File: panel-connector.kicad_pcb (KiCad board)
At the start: 2 copper layers, 95.9 x 90.2 mm, 201 parts, among them J1 PC104-8BIT, J105 MOLEX_FFC-14, J2 PC104PTH, J200 MOLEX_FFC-14, J201 CONN-TAB, J202 CONN-TAB, J203 CONN-TAB, J204 CONN-TAB, J210 MOLEX_FFC-14, J211 CONN-TAB, J212 CONN-TAB, J213 CONN-TAB, J214 CONN-TAB, J220 MOLEX_FFC-14, J221 CONN-TAB, J222 CONN-TAB, J223 CONN-TAB, J224 CONN-TAB, J230 MOLEX_FFC-14, J231 CONN-TAB, J232 CONN-TAB, J233 CONN-TAB, J234 CONN-TAB, J3 PC104PTH, J4 PC104PTH, J5 PC104PTH, J6 OEM719, U100 SPV1040, U110 SPV1040, U120 SPV1040, U130 SPV1040, U140 SPV1040, U150 SPV1040, U160 SPV1040, U170 SPV1040, U200 ADG728, U210 ADG728, U220 ADG728, U230 ADG728

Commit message: placed mppt circuits
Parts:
- C100, C101, C102, C103, C104, C105, C110, C111, C112, C113, C114, C115, C120, C121, C122, C123, C124, C125, C130, C131, C132, C133, C134, C135, C140, C141, C142, C143, C144, C145, C150, C151, C152, C153, C154, C155, C160, C161, C162, C163, C164, C165, C170, C171, C172, C173, C174, C175, C211, C212, C221, C222, C231, C232, D100, D110, D120, D130, D140, D150, D160, D170, J105, J200, J201, J202, J203, J204, J210, J220, J230, L100, L110, L120, L130, L140, L150, L160, L170, R100, R101, R102, R103, R104, R105, R106, R110, R111, R112, R113, R114, R115, R116, R120, R121, R122, R123, R124, R125, R126, R130, R131, R132, R133, R134, R135, R136, R140, R141, R142, R143, R144, R145, R146, R150, R151, R152, R153, R154, R155, R156, R160, R161, R162, R163, R164, R165, R166, R170, R171, R172, R173, R174, R175, R176, R210, R211, R212, R213, R214, R215, R220, R221, R222, R223, R224, R225, R230, R231, R232, R233, R234, R235, U100, U110, U120, U130, U140, U150, U160, U170, U210, U220, U230: moved to B.Cu
- moved R106 198.6 mm to (159.0, 99.6), turned to 270 degrees
- moved C104 198.4 mm to (161.9, 102.3), turned to 180 degrees
- moved C102 195.9 mm to (160.9, 99.6), turned to 270 degrees
- moved R103 193.4 mm to (159.8, 96.7), turned to 0 degrees
- moved R105 193.1 mm to (162.9, 99.6), turned to 90 degrees
- moved R102 190.7 mm to (159.8, 94.8), turned to 0 degrees
- moved R104 189.7 mm to (167.7, 101.9), turned to 180 degrees
- moved C103 187.9 mm to (162.7, 95.7), turned to 270 degrees
- moved C105 185.9 mm to (168.2, 99.8), turned to 180 degrees
- moved U100 181.3 mm to (168.1, 96.4), turned to 180 degrees
- moved D100 181.0 mm to (172.6, 100.7), turned to 180 degrees
- moved R101 180.7 mm to (166.0, 93.8), turned to 0 degrees
- moved D160 178.3 mm to (173.7, 56.4), turned to 270 degrees
- moved L160 176.3 mm to (168.0, 54.1), turned to 0 degrees
- moved R164 176.2 mm to (174.9, 61.3), turned to 270 degrees
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- renumbered R201'1 to R201
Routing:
- net (no net): track 26.0 -> 0.00 mm
- net GND: track 36.9 -> 55.9 mm, vias 32 -> 48
- net /3V3: track 0.00 -> 11.9 mm
- net /Port_X-/A1: track 0.00 -> 3.52 mm
- net /Port_Y-/A1: track 0.00 -> 3.52 mm
- net /Port_X+/A1: track 0.00 -> 3.52 mm
- net /Port_Y+/A1: track 0.00 -> 3.52 mm
- net /Port_Y-/A0: track 0.00 -> 3.38 mm
- net /Port_X-/A0: track 0.00 -> 3.38 mm
- net /Port_Y+/A0: track 0.00 -> 3.38 mm
- net /Port_X+/A0: track 0.00 -> 3.38 mm
- net /SENSOR_Y+: track 0.00 -> 3.00 mm
- net /SENSOR_X-: track 0.00 -> 3.00 mm
- net /SENSOR_Y-: track 0.00 -> 3.00 mm
- net /SENSOR_X+: track 0.00 -> 3.00 mm
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- added copper zone on B.Cu, net /MPPT_X+_1/LX
- added copper zone on B.Cu, net /MPPT_X+_1/MPPT_OUT
- added copper zone on B.Cu, net /MPPT_X+_1/PV+
- added copper zone on B.Cu, net /MPPT_X+_1/VOUT+
- added copper zone on B.Cu, net /MPPT_X+_2/LX
- added copper zone on B.Cu, net /MPPT_X+_2/MPPT_OUT
- added copper zone on B.Cu, net /MPPT_X+_2/PV+
- added copper zone on B.Cu, net /MPPT_X-_1/LX
- added copper zone on B.Cu, net /MPPT_X-_1/MPPT_OUT
- added copper zone on B.Cu, net /MPPT_X-_1/PV+
- added copper zone on B.Cu, net /MPPT_X-_2/LX
- added copper zone on B.Cu, net /MPPT_X-_2/MPPT_OUT
- added copper zone on B.Cu, net /MPPT_X-_2/PV+
- added copper zone on B.Cu, net /MPPT_Y+_1/LX
- added copper zone on B.Cu, net /MPPT_Y+_1/MPPT_OUT
- added copper zone on B.Cu, net /MPPT_Y+_1/PV+
- added copper zone on B.Cu, net /MPPT_Y+_2/LX
- added copper zone on B.Cu, net /MPPT_Y+_2/MPPT_OUT
- added copper zone on B.Cu, net /MPPT_Y+_2/PV+
- added copper zone on B.Cu, net /MPPT_Y-_1/LX
- added copper zone on B.Cu, net /MPPT_Y-_1/MPPT_OUT
- added copper zone on B.Cu, net /MPPT_Y-_1/PV+
- added copper zone on B.Cu, net /MPPT_Y-_2/LX
- added copper zone on B.Cu, net /MPPT_Y-_2/MPPT_OUT
- added copper zone on B.Cu, net /MPPT_Y-_2/PV+
- added copper zone on F.Cu, net GND
- removed copper zone on F.Cu, net /MPPT_X+_1/LX
- removed copper zone on F.Cu, net /MPPT_X+_1/MPPT_OUT
- removed copper zone on F.Cu, net /MPPT_X+_1/PV+
- removed copper zone on F.Cu, net /MPPT_X+_1/VOUT+
- removed copper zone on F.Cu, net /MPPT_X+_2/LX
- removed copper zone on F.Cu, net /MPPT_X+_2/MPPT_OUT
- removed copper zone on F.Cu, net /MPPT_X+_2/PV+
- removed copper zone on F.Cu, net /MPPT_X-_1/LX
- removed copper zone on F.Cu, net /MPPT_X-_1/MPPT_OUT
- removed copper zone on F.Cu, net /MPPT_X-_1/PV+
- removed copper zone on F.Cu, net /MPPT_X-_2/LX
- removed copper zone on F.Cu, net /MPPT_X-_2/MPPT_OUT
- removed copper zone on F.Cu, net /MPPT_X-_2/PV+
- removed copper zone on F.Cu, net /MPPT_Y+_1/LX
- removed copper zone on F.Cu, net /MPPT_Y+_1/MPPT_OUT
- removed copper zone on F.Cu, net /MPPT_Y+_1/PV+
- removed copper zone on F.Cu, net /MPPT_Y+_2/LX
- removed copper zone on F.Cu, net /MPPT_Y+_2/MPPT_OUT
- removed copper zone on F.Cu, net /MPPT_Y+_2/PV+
- removed copper zone on F.Cu, net /MPPT_Y-_1/LX
- removed copper zone on F.Cu, net /MPPT_Y-_1/MPPT_OUT
- removed copper zone on F.Cu, net /MPPT_Y-_1/PV+
- removed copper zone on F.Cu, net /MPPT_Y-_2/LX
- removed copper zone on F.Cu, net /MPPT_Y-_2/MPPT_OUT
- removed copper zone on F.Cu, net /MPPT_Y-_2/PV+
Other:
- board text removed: "GPS Coax slot location and dimentions are provisional. Consider structural integrity of the board with cables connected."

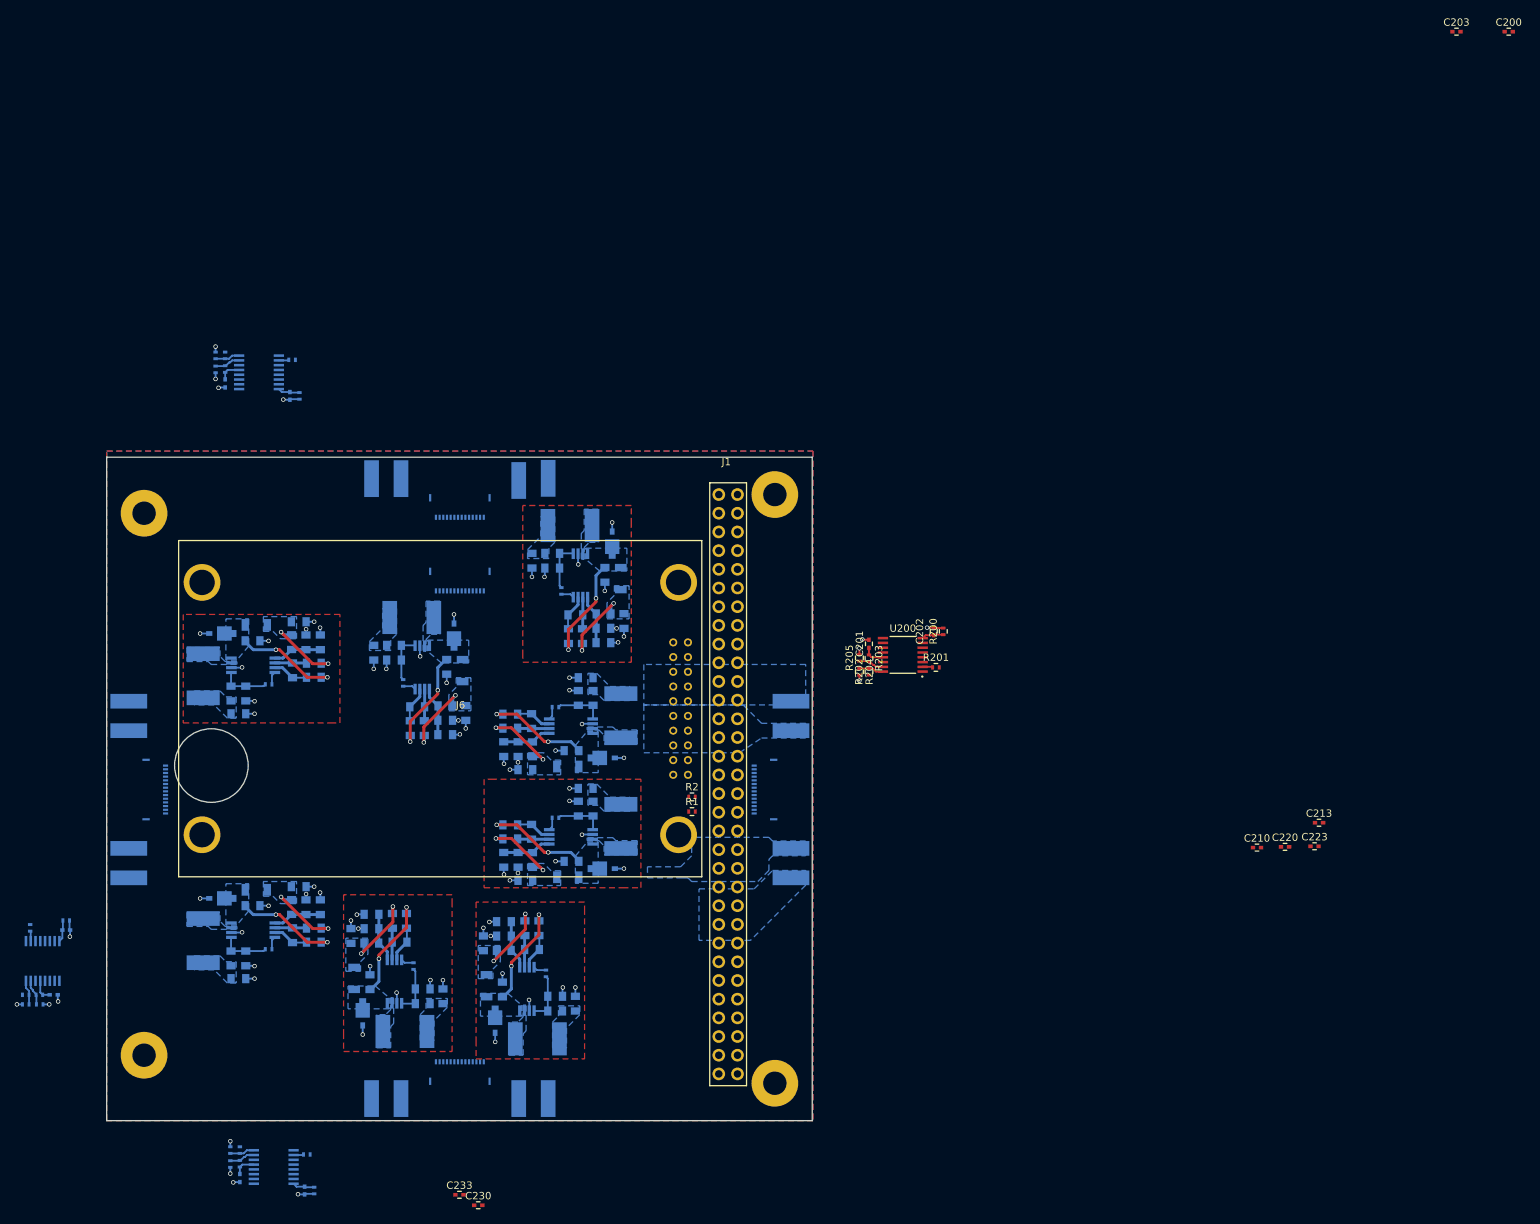
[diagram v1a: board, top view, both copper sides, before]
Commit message: routing complete except for GPS_RST
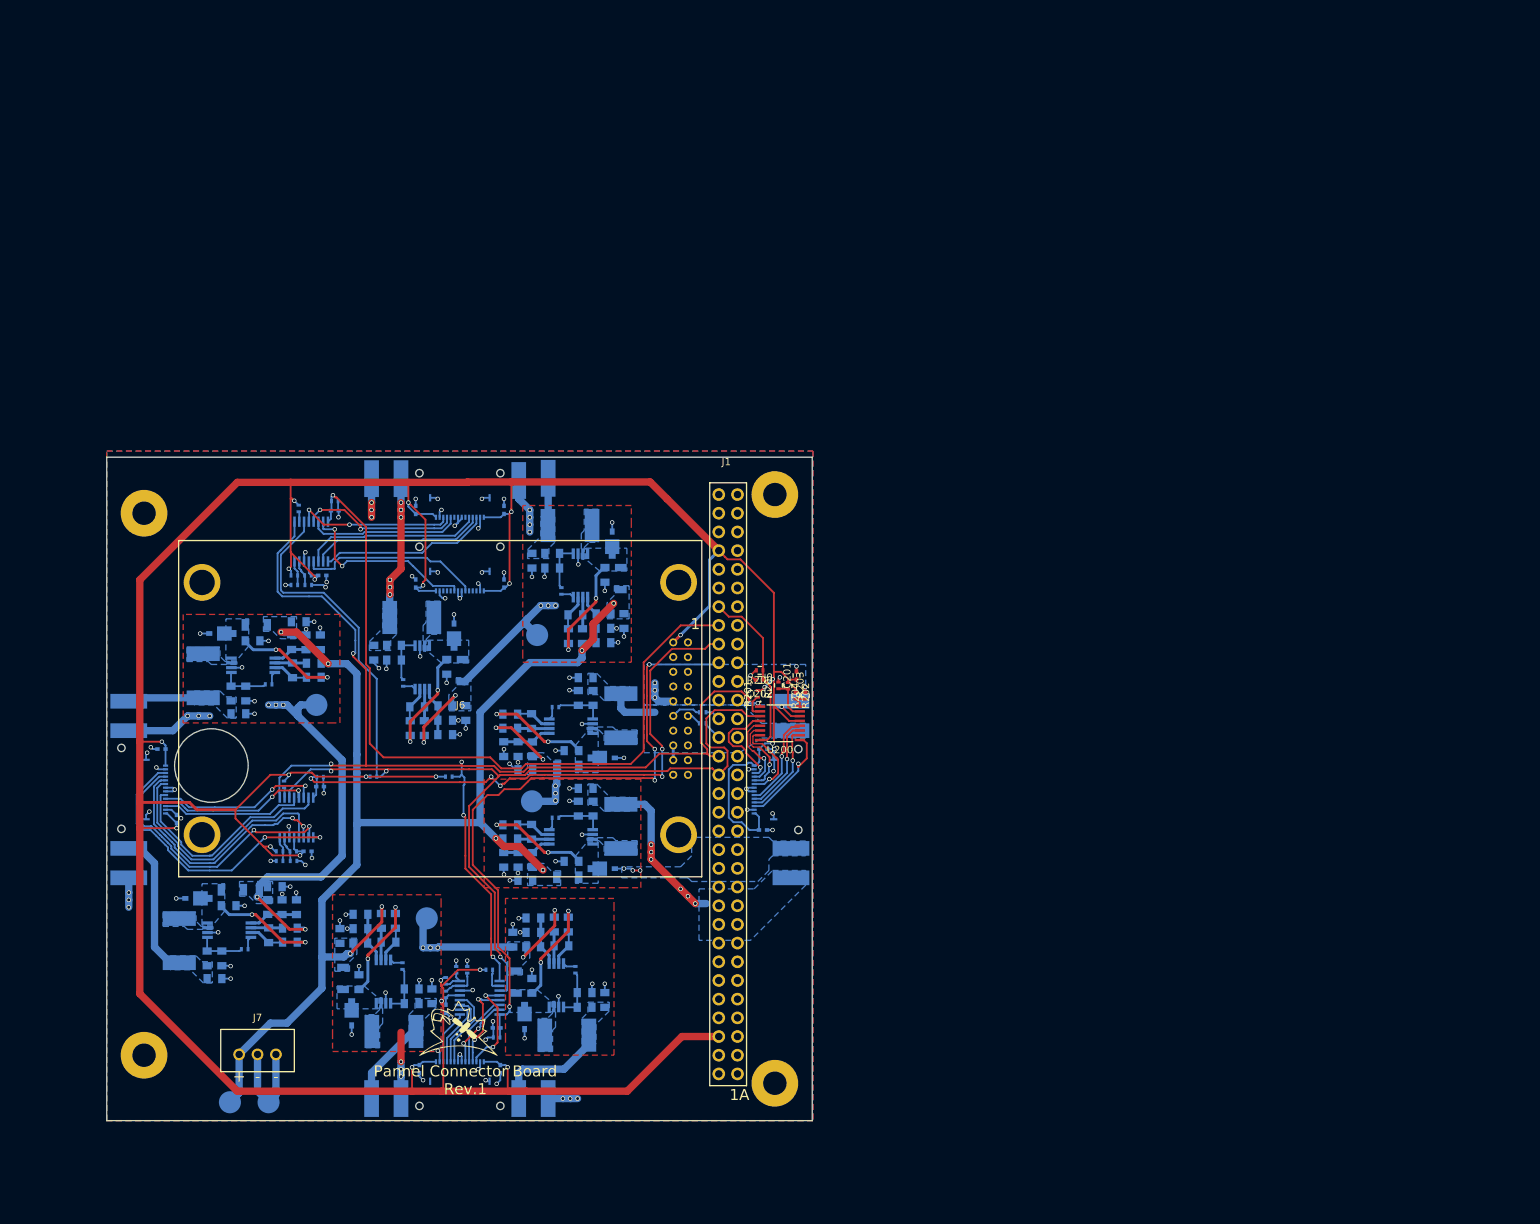
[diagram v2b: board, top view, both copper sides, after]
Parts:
- added C1: DNP, Capacitors_SMD:C_0402, B.Cu at (159.0, 62.0)
- added C2: DNP, Capacitors_SMD:C_0402, B.Cu at (147.0, 62.0)
- added G***: LOGO, SFUSat:SFUSat_15mm_2, F.Cu at (152.8, 122.5)
- added J10: TEST_1P, SFUSat:Measurement_Point_Round-SMD-Pad_Big, B.Cu at (163.5, 69.0)
- added J11: TEST_1P, SFUSat:Measurement_Point_Round-SMD-Pad_Big, B.Cu at (148.5, 107.5)
- added J12: TEST_1P, SFUSat:Measurement_Point_Round-SMD-Pad_Big, B.Cu at (121.8, 132.5)
- added J13: TEST_1P, SFUSat:Measurement_Point_Round-SMD-Pad_Big, B.Cu at (127.0, 132.5)
- added J7: B3B-XH-A(LF)(SN), SFUSat:B3B-XH-A, F.Cu at (125.5, 126.0)
- added J8: TEST_1P, SFUSat:Measurement_Point_Round-SMD-Pad_Big, B.Cu at (162.8, 91.6)
- added J9: TEST_1P, SFUSat:Measurement_Point_Round-SMD-Pad_Big, B.Cu at (133.5, 78.5)
- added R3: 0R, SFUSat-res:R_0402, B.Cu at (186.0, 79.5)
- added R4: 0R, SFUSat-res:R_0402, B.Cu at (186.0, 81.0)
- added REF**: NPTH-1mm, SFUSat:NPTH-1mm, B.Cu at (199.0, 95.5)
- added REF**: NPTH-1mm, SFUSat:NPTH-1mm, B.Cu at (107.0, 95.3)
- added REF**: NPTH-1mm, SFUSat:NPTH-1mm, B.Cu at (199.0, 84.5)
- added REF**: NPTH-1mm, SFUSat:NPTH-1mm, B.Cu at (158.5, 57.0)
- added REF**: NPTH-1mm, SFUSat:NPTH-1mm, B.Cu at (147.5, 57.0)
- added REF**: NPTH-1mm, SFUSat:NPTH-1mm, B.Cu at (158.5, 47.0)
- added REF**: NPTH-1mm, SFUSat:NPTH-1mm, B.Cu at (147.5, 47.0)
- added REF**: NPTH-1mm, SFUSat:NPTH-1mm, B.Cu at (158.5, 133.0)
- added REF**: NPTH-1mm, SFUSat:NPTH-1mm, B.Cu at (147.5, 133.0)
- added REF**: NPTH-1mm, SFUSat:NPTH-1mm, B.Cu at (107.0, 84.3)
- C200, C203, C210, C213, C220, C223, C230, C233: moved to B.Cu
- R1, R2: value R -> DNP; moved to B.Cu
- moved C213 157.6 mm to (112.5, 84.5), turned to 180 degrees
- moved C200 148.5 mm to (194.2, 95.5), turned to 180 degrees
- moved C210 146.9 mm to (114.5, 94.0), turned to 270 degrees
- moved C203 135.6 mm to (194.2, 84.5)
- moved C220 121.5 mm to (147.5, 128.0), turned to 90 degrees
- moved C223 114.7 mm to (158.5, 128.0), turned to 270 degrees
- moved C230 94.6 mm to (159.0, 52.0), turned to 270 degrees
- moved C233 93.3 mm to (147.0, 52.0), turned to 90 degrees
- moved R1 43.6 mm to (141.2, 88.2)
- moved R225 41.6 mm to (154.0, 114.5), turned to 90 degrees
- moved C211 39.6 mm to (132.3, 98.4)
- moved U210 39.6 mm to (130.8, 93.8)
- moved C212 39.6 mm to (134.0, 89.6)
- moved R210 39.6 mm to (134.0, 88.3)
- moved R211 39.6 mm to (129.1, 89.3)
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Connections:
- net Net-(J6-Pad5) renamed /GPS_RST
- J1 pad 19B: Net-(J1-Pad19B) -> /GPS_TX
- J1 pad 20B: Net-(J1-Pad20B) -> /GPS_RX
- J1 pad 29B: Net-(J1-Pad29B) -> /3V3
- J1 pad 3B: Net-(J1-Pad3B) -> /3V3
- J105 pad 11: Z+D7 -> Net-(J105-Pad11)
- J105 pad 12: Z+D8 -> Net-(J105-Pad12)
- J105 pad 6: Net-(J105-Pad6) -> Z+D_A
- J105 pad 9: Net-(J105-Pad9) -> Z+D_B
- J200 pad 11: Z+D7 -> /Port_X+/D7
- J200 pad 12: Z+D8 -> /Port_X+/D8
- J200 pad 6: /Port_X+/D4 -> Z+D_A
- J200 pad 9: /Port_X+/D5 -> Z+D_B
- J210 pad 11: Z+D7 -> /Port_X-/D7
- J210 pad 12: Z+D8 -> /Port_X-/D8
- J210 pad 6: /Port_X-/D4 -> Z+D_A
- J210 pad 9: /Port_X-/D5 -> Z+D_B
- J220 pad 11: Z+D7 -> /Port_Y+/D7
- J220 pad 12: Z+D8 -> /Port_Y+/D8
- J220 pad 6: /Port_Y+/D4 -> Z+D_A
- J220 pad 9: /Port_Y+/D5 -> Z+D_B
- J230 pad 11: Z+D7 -> /Port_Y-/D7
- J230 pad 12: Z+D8 -> /Port_Y-/D8
- J230 pad 6: /Port_Y-/D4 -> Z+D_A
- J230 pad 9: /Port_Y-/D5 -> Z+D_B
- U200 pad 10: Z+D7 -> /Port_X+/D7
- U200 pad 12: /Port_X+/D5 -> Z+D_B
- U200 pad 7: /Port_X+/D4 -> Z+D_A
- U200 pad 9: Z+D8 -> /Port_X+/D8
- U210 pad 10: Z+D7 -> /Port_X-/D7
- U210 pad 12: /Port_X-/D5 -> Z+D_B
- U210 pad 7: /Port_X-/D4 -> Z+D_A
- U210 pad 9: Z+D8 -> /Port_X-/D8
- U220 pad 10: Z+D7 -> /Port_Y+/D7
- U220 pad 12: /Port_Y+/D5 -> Z+D_B
- U220 pad 7: /Port_Y+/D4 -> Z+D_A
- U220 pad 9: Z+D8 -> /Port_Y+/D8
- U230 pad 10: Z+D7 -> /Port_Y-/D7
- U230 pad 12: /Port_Y-/D5 -> Z+D_B
- U230 pad 7: /Port_Y-/D4 -> Z+D_A
- U230 pad 9: Z+D8 -> /Port_Y-/D8
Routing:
- net /3V3: track 11.9 -> 501.7 mm, vias 0 -> 23
- net /SDA: track 0.00 -> 161.3 mm, vias 0 -> 3
- net /SCL: track 0.00 -> 159.3 mm, vias 0 -> 7
- net /MPPT_X+_1/VOUT+: track 43.4 -> 171.5 mm
- net /SENSOR_Y-: track 3.00 -> 103.8 mm, vias 0 -> 1
- net GND: track 55.9 -> 146.8 mm, vias 48 -> 98
- net /SENSOR_Y+: track 3.00 -> 86.7 mm, vias 0 -> 4
- net Z+D_B: track 0.00 -> 82.2 mm, vias 0 -> 1
- net Z+D_A: track 0.00 -> 77.7 mm, vias 0 -> 5
- net /SENSOR_X-: track 3.00 -> 79.3 mm, vias 0 -> 5
- net /MPPT_X-_1/PV-: track 20.1 -> 76.9 mm, vias 10 -> 16
- net /Port_X-/D8: track 0.00 -> 39.7 mm, vias 0 -> 2
- net /Port_X-/D7: track 0.00 -> 38.0 mm, vias 0 -> 2
- net /Port_X-/D6: track 0.00 -> 34.5 mm, vias 0 -> 2
- net /MPPT_Y-_1/PV-: track 20.1 -> 47.6 mm, vias 10 -> 17
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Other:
- board text added: "+"
- board text added: "-"
- board text added: "1"
- board text added: "1A"
- board text added: "Pannel Connector Board Rev.1"

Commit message: routing complete
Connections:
- J1 pad 9B: (no net) -> /GPS_RST
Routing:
- net /GPS_RST: track 0.00 -> 37.4 mm, vias 0 -> 2

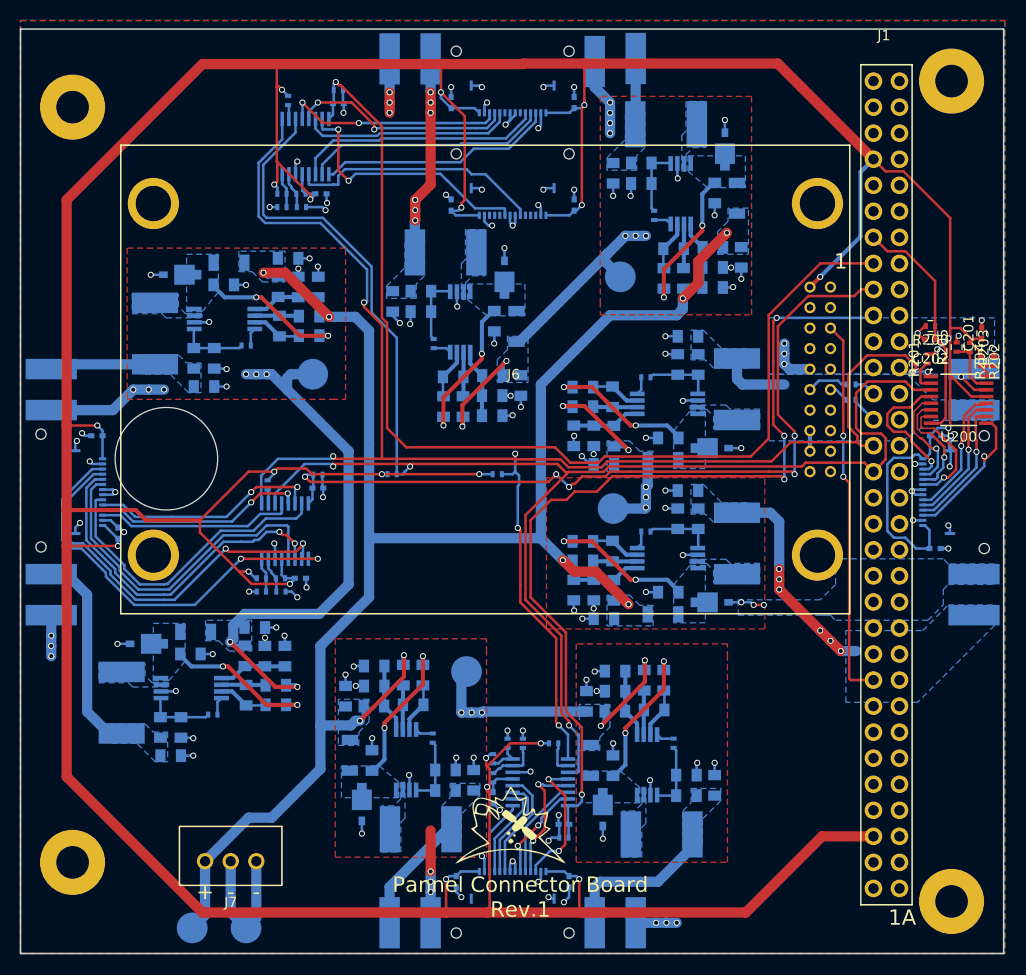
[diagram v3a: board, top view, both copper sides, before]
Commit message: optimized reference layout
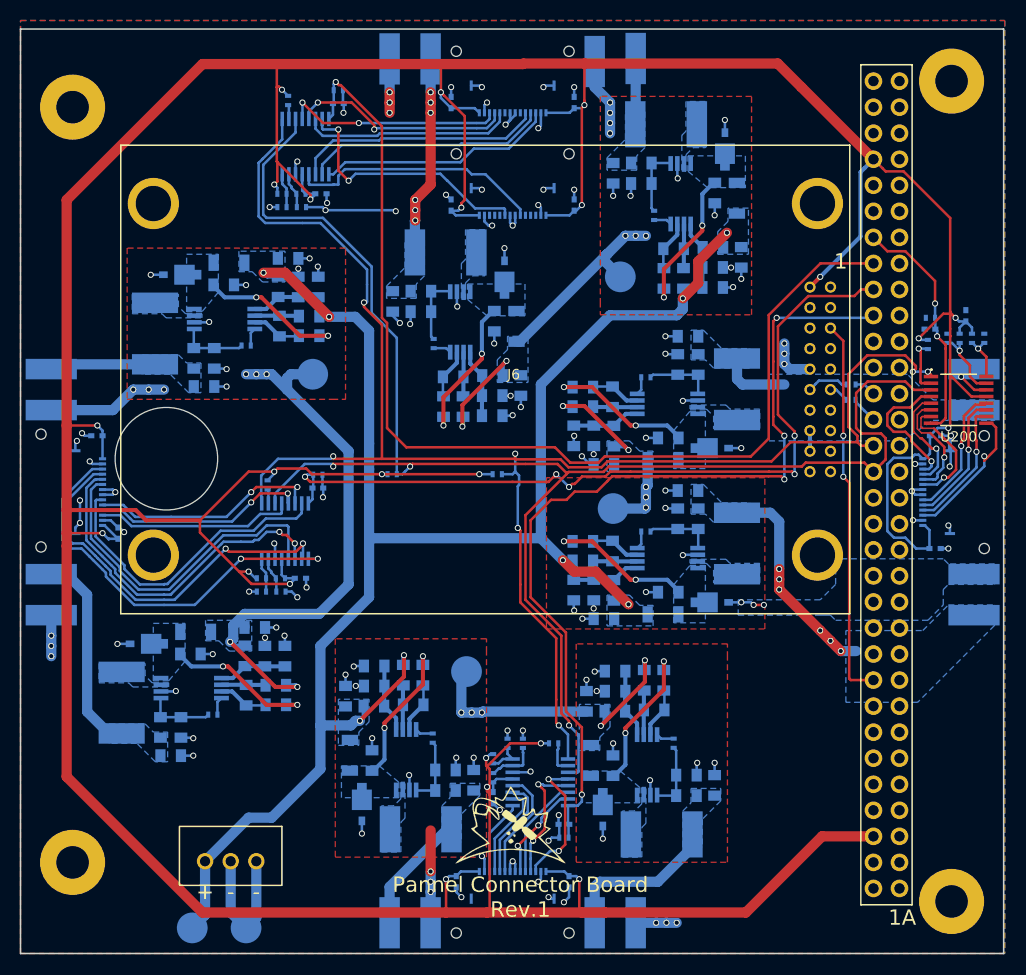
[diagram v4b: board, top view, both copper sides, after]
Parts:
- C201, C202, R200, R202, R203, R204, R205: moved to B.Cu
- R201: value R -> 0R; moved to B.Cu
- R211, R221, R231: value R -> 0R
- moved R204 2.44 mm to (199.0, 75.0)
- moved R202 2.41 mm to (197.8, 75.0)
- moved C201 2.30 mm to (197.2, 72.8)
- moved R201 1.40 mm to (193.5, 75.6)
- moved R203 1.35 mm to (196.6, 75.0)
- moved R205 1.24 mm to (195.4, 75.0)
- moved C202 1.00 mm to (193.7, 74.1)
- moved R200 0.80 mm to (193.8, 73.0)
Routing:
- net GND: track 146.8 -> 151.6 mm, vias 98 -> 96
- net /Port_X+/A0: track 2.55 -> 4.71 mm, vias 0 -> 1
- net /Port_X+/!RESET: track 3.26 -> 5.37 mm, vias 0 -> 1
- net /Port_X+/A1: track 5.66 -> 7.07 mm, vias 0 -> 1
- net /3V3: track 501.7 -> 502.2 mm
- net /SENSOR_X+: vias 0 -> 2
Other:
- board text added: "1xx"
- board text added: "2xx"
- board text added: "C0"
- board text added: "C1"
- board text added: "C2"
- board text added: "C3"
- board text added: "C4"
- board text added: "C5"
- board text added: "D0"
- board text added: "L0"
- board text added: "PV-"
- board text added: "R0"
- board text added: "R1"
- board text added: "R2"
- board text added: "R3"
- board text added: "R4"
- board text added: "R5"
- board text added: "R6"
- board text added: "U0"
